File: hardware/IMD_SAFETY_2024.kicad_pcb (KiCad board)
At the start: 4 copper layers, 60 x 40 mm, 4 parts

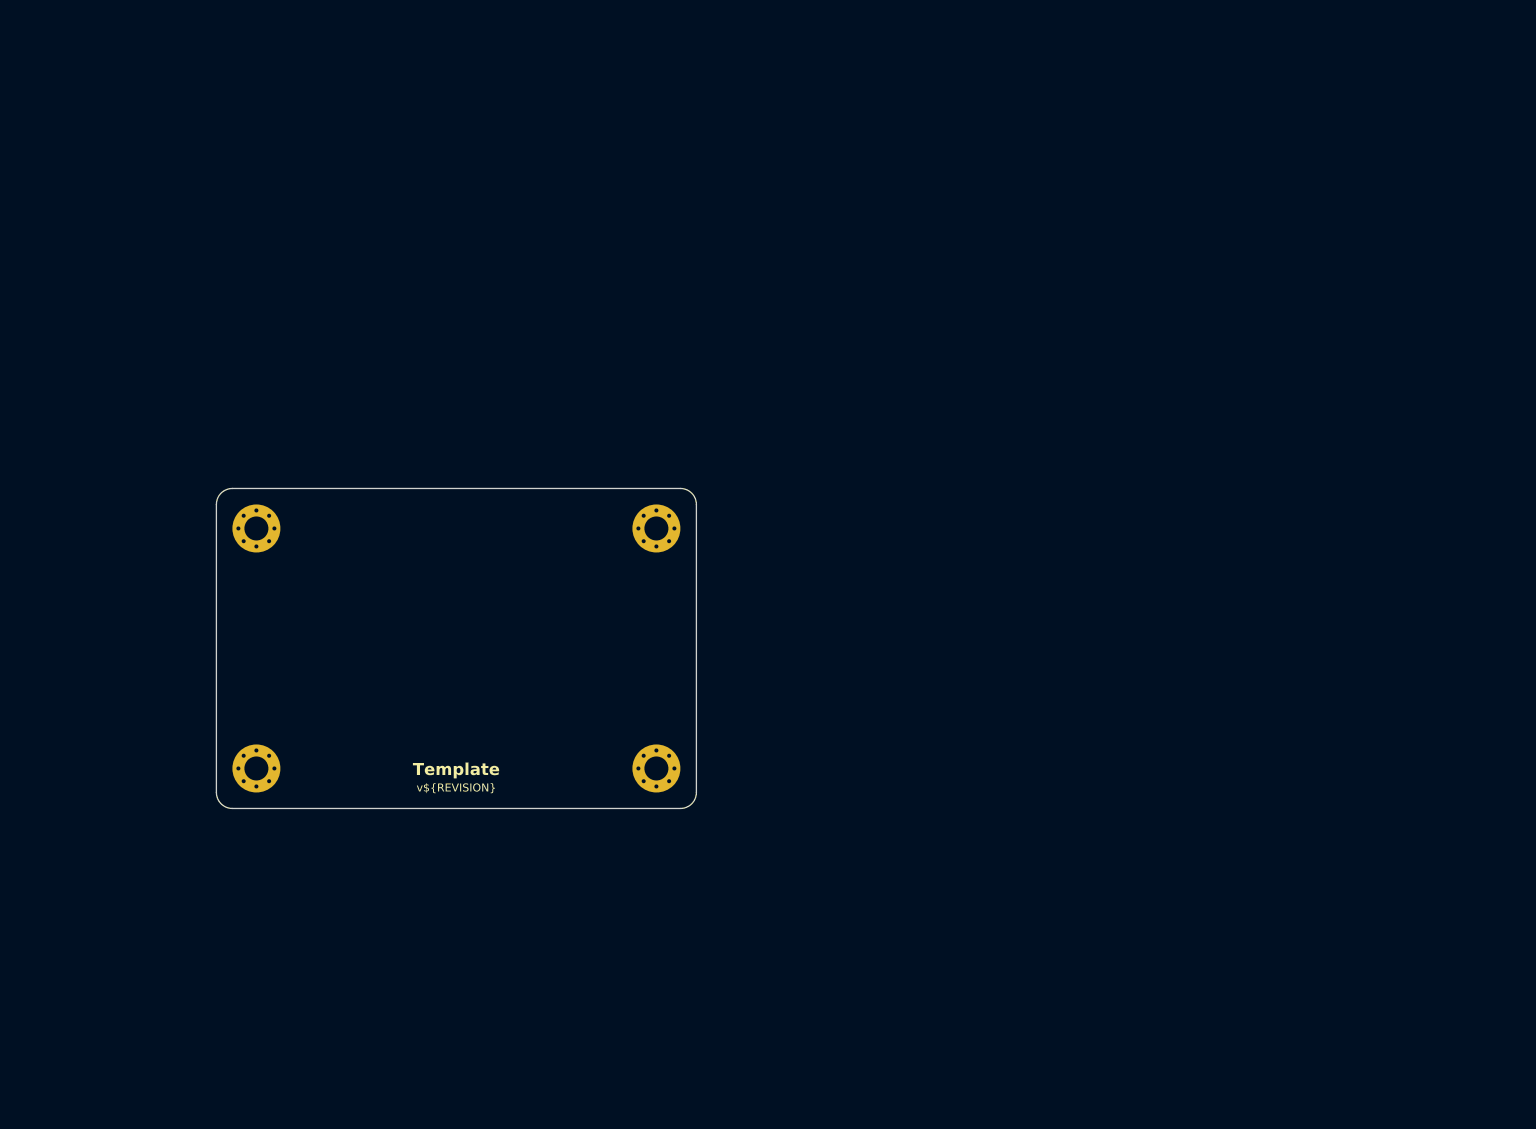
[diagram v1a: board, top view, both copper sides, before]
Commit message: Passives footprint assignment
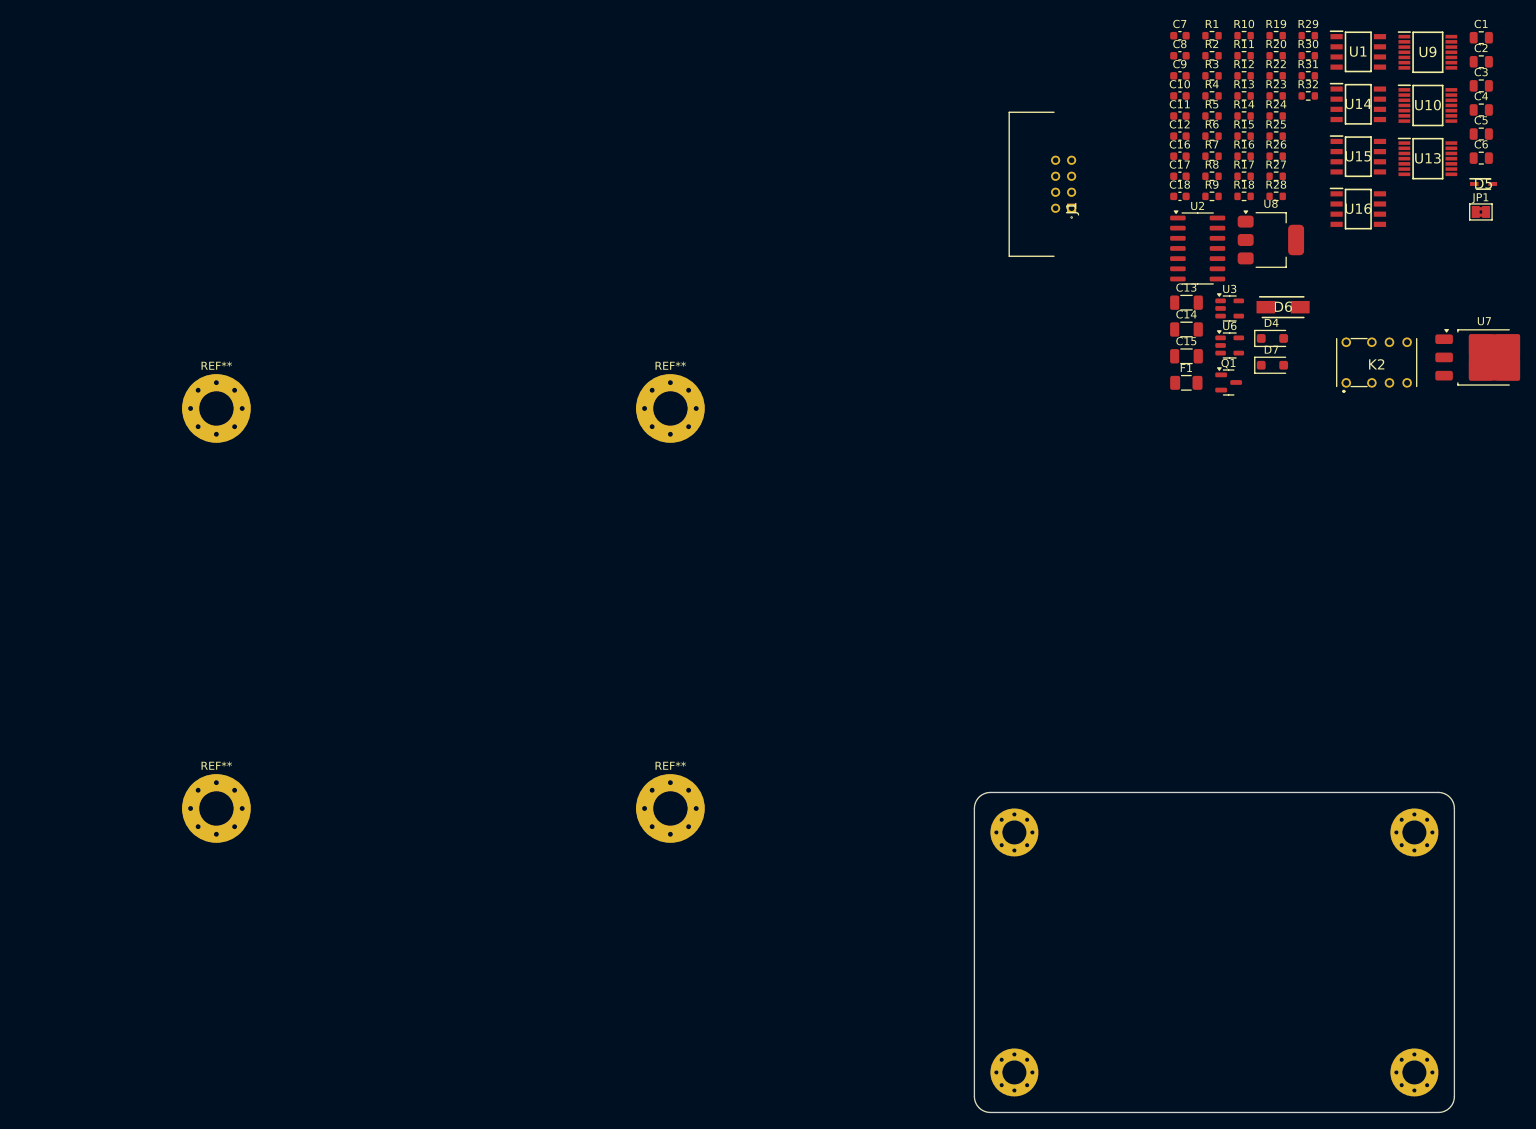
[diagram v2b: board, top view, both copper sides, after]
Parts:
- added C1: 1u/35V, Capacitor_SMD:C_0805_2012Metric, F.Cu at (274.1, 19.7)
- added C10: 100nF/35V, Capacitor_SMD:C_0603_1608Metric, F.Cu at (236.4, 26.9)
- added C11: 100nF/35V, Capacitor_SMD:C_0603_1608Metric, F.Cu at (236.4, 29.4)
- added C12: 100nF/35V, Capacitor_SMD:C_0603_1608Metric, F.Cu at (236.4, 32.0)
- added C13: 47uF, Capacitor_SMD:C_1206_3216Metric, F.Cu at (237.3, 52.8)
- added C14: 22u, Capacitor_SMD:C_1206_3216Metric, F.Cu at (237.3, 56.1)
- added C15: 10u, Capacitor_SMD:C_1206_3216Metric, F.Cu at (237.3, 59.5)
- added C16: 100nF/35V, Capacitor_SMD:C_0603_1608Metric, F.Cu at (236.4, 34.5)
- added C17: 100nF/35V, Capacitor_SMD:C_0603_1608Metric, F.Cu at (236.4, 37.0)
- added C18: 100nF/35V, Capacitor_SMD:C_0603_1608Metric, F.Cu at (236.4, 39.5)
- added C2: 1u/35V, Capacitor_SMD:C_0805_2012Metric, F.Cu at (274.1, 22.7)
- added C3: 1u/35V, Capacitor_SMD:C_0805_2012Metric, F.Cu at (274.1, 25.7)
- added C4: 1u/35V, Capacitor_SMD:C_0805_2012Metric, F.Cu at (274.1, 28.7)
- added C5: 1u/35V, Capacitor_SMD:C_0805_2012Metric, F.Cu at (274.1, 31.7)
- added C6: 1u/35V, Capacitor_SMD:C_0805_2012Metric, F.Cu at (274.1, 34.7)
- added C7: 100nF/35V, Capacitor_SMD:C_0603_1608Metric, F.Cu at (236.4, 19.4)
- added C8: 100nF/35V, Capacitor_SMD:C_0603_1608Metric, F.Cu at (236.4, 21.9)
- added C9: 100nF/35V, Capacitor_SMD:C_0603_1608Metric, F.Cu at (236.4, 24.4)
- added D4: SD103BW, Diode_SMD:D_SOD-123F, F.Cu at (248.0, 57.2)
- added D5: SD24-01FTG, Samacsys:SOD2613X114N, F.Cu at (274.4, 37.9)
- added D6: SK36A-LTP, Samacsys:DIOM5226X244N, F.Cu at (249.3, 53.3)
- added D7: SD103BW, Diode_SMD:D_SOD-123F, F.Cu at (248.0, 60.6)
- added F1: 500mA, Fuse:Fuse_1206_3216Metric, F.Cu at (237.2, 62.8)
- added J1: Main- M80-5300842, Samacsys:M80-53008YY, F.Cu at (222.9, 41.0)
- added JP1: Output_Jumper, Jumper:SolderJumper-2_P1.3mm_Bridged2Bar_Pad1.0x1.5mm, F.Cu at (274.1, 41.4)
- added K2: TE AXICOM IM07DTS, footprints:IM23TS, F.Cu at (261.0, 60.5)
- added Q1: 2N7002, Package_TO_SOT_SMD:SOT-23, F.Cu at (242.5, 62.8)
- added R1: 2.2K, Resistor_SMD:R_0603_1608Metric, F.Cu at (240.5, 19.4)
- added R10: 100k, Resistor_SMD:R_0603_1608Metric, F.Cu at (244.5, 19.4)
- added R11: 14.3k, Resistor_SMD:R_0603_1608Metric, F.Cu at (244.5, 21.9)
- added R12: 150K, Resistor_SMD:R_0603_1608Metric, F.Cu at (244.5, 24.4)
- added R13: 33K, Resistor_SMD:R_0603_1608Metric, F.Cu at (244.5, 26.9)
- added R14: 0k, Resistor_SMD:R_0603_1608Metric, F.Cu at (244.5, 29.4)
- added R15: 400K, Resistor_SMD:R_0603_1608Metric, F.Cu at (244.5, 32.0)
- added R16: 100K, Resistor_SMD:R_0603_1608Metric, F.Cu at (244.5, 34.5)
- added R17: 2.2K, Resistor_SMD:R_0603_1608Metric, F.Cu at (244.5, 37.0)
- added R18: 2.2K, Resistor_SMD:R_0603_1608Metric, F.Cu at (244.5, 39.5)
- added R19: 1K, Resistor_SMD:R_0603_1608Metric, F.Cu at (248.5, 19.4)
- added R2: 2.2K, Resistor_SMD:R_0603_1608Metric, F.Cu at (240.5, 21.9)
- added R20: 10k, Resistor_SMD:R_0603_1608Metric, F.Cu at (248.5, 21.9)
- added R22: 100k, Resistor_SMD:R_0603_1608Metric, F.Cu at (248.5, 24.4)
- added R23: 330R, Resistor_SMD:R_0603_1608Metric, F.Cu at (248.5, 26.9)
- added R24: 20k, Resistor_SMD:R_0603_1608Metric, F.Cu at (248.5, 29.4)
- added R25: 30k, Resistor_SMD:R_0603_1608Metric, F.Cu at (248.5, 32.0)
- added R26: 120k, Resistor_SMD:R_0603_1608Metric, F.Cu at (248.5, 34.5)
- added R27: 20k, Resistor_SMD:R_0603_1608Metric, F.Cu at (248.5, 37.0)
- added R28: 10k, Resistor_SMD:R_0603_1608Metric, F.Cu at (248.5, 39.5)
- added R29: 2.2K, Resistor_SMD:R_0603_1608Metric, F.Cu at (252.5, 19.4)
- added R3: 10K, Resistor_SMD:R_0603_1608Metric, F.Cu at (240.5, 24.4)
- added R30: 100K, Resistor_SMD:R_0603_1608Metric, F.Cu at (252.5, 21.9)
- added R31: 10k, Resistor_SMD:R_0603_1608Metric, F.Cu at (252.5, 24.4)
- added R32: 1M, Resistor_SMD:R_0603_1608Metric, F.Cu at (252.5, 26.9)
- added R4: 10K, Resistor_SMD:R_0603_1608Metric, F.Cu at (240.5, 26.9)
- added R5: 2.2K, Resistor_SMD:R_0603_1608Metric, F.Cu at (240.5, 29.4)
- added R6: 2.2K, Resistor_SMD:R_0603_1608Metric, F.Cu at (240.5, 32.0)
- added R7: 47K, Resistor_SMD:R_0603_1608Metric, F.Cu at (240.5, 34.5)
- added R8: 47K, Resistor_SMD:R_0603_1608Metric, F.Cu at (240.5, 37.0)
- added R9: 300K, Resistor_SMD:R_0603_1608Metric, F.Cu at (240.5, 39.5)
- added REF**: MountingHole_4.3mm_M4_Pad_Via, MountingHole:MountingHole_4.3mm_M4_Pad_Via, F.Cu at (116.0, 66.0)
- added REF**: MountingHole_4.3mm_M4_Pad_Via, MountingHole:MountingHole_4.3mm_M4_Pad_Via, F.Cu at (116.0, 116.0)
- added REF**: MountingHole_4.3mm_M4_Pad_Via, MountingHole:MountingHole_4.3mm_M4_Pad_Via, F.Cu at (172.8, 66.0)
- added REF**: MountingHole_4.3mm_M4_Pad_Via, MountingHole:MountingHole_4.3mm_M4_Pad_Via, F.Cu at (172.8, 116.0)
- added U1: LM393, Samacsys:SOIC127P600X175-8N, F.Cu at (258.7, 21.4)
- added U10: 74HCS08, Samacsys:SOP65P640X120-14N, F.Cu at (267.4, 28.1)
- added U13: 74HC74, Samacsys:SOP65P640X120-14N, F.Cu at (267.4, 34.8)
- added U14: LM393, Samacsys:SOIC127P600X175-8N, F.Cu at (258.7, 28.0)
- added U15: LM393, Samacsys:SOIC127P600X175-8N, F.Cu at (258.7, 34.5)
- added U16: LM393, Samacsys:SOIC127P600X175-8N, F.Cu at (258.7, 41.1)
- added U2: 74AC04SC, Package_SO:SOIC-14_3.9x8.7mm_P1.27mm, F.Cu at (238.7, 46.0)
- added U3: 74LVC1G79, Package_TO_SOT_SMD:SOT-23-5, F.Cu at (242.7, 53.5)
- added U6: 74LVC1G79, Package_TO_SOT_SMD:SOT-23-5, F.Cu at (242.7, 58.1)
- added U7: MC78M12CDTG, Package_TO_SOT_SMD:TO-252-3_TabPin2, F.Cu at (274.5, 59.6)
- added U8: LM1117IMP-5.0, Package_TO_SOT_SMD:SOT-223-3_TabPin2, F.Cu at (247.8, 44.9)
- added U9: 74HCS32, Samacsys:SOP65P640X120-14N, F.Cu at (267.4, 21.5)
- moved REF** 102.1 mm to (265.8, 119.0)
- moved REF** 102.1 mm to (215.8, 149.0)
- moved REF** 102.1 mm to (215.8, 119.0)
- moved REF** 102.1 mm to (265.8, 149.0)
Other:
- board text added: "BETWEEN HORIZONTAL HOLES: 56,75mm"
- board text added: "BETWEEN VERTICAL HOLES: 50mm"
- board text removed: "Template"
- board text removed: "v${REVISION}"

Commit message: WIP Layout
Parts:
- removed the REF** at (265.8, 119.0)
- removed the REF** at (215.8, 149.0)
- removed the REF** at (215.8, 119.0)
- removed the REF** at (265.8, 149.0)
- added C19: 100nF/35V, Capacitor_SMD:C_0603_1608Metric, F.Cu at (136.7, 93.1)
- added C20: 100nF/35V, Capacitor_SMD:C_0603_1608Metric, F.Cu at (130.2, 92.9)
- added C21: TBD, Capacitor_SMD:C_1206_3216Metric, F.Cu at (146.4, 81.2)
- added R33: 10k, Resistor_SMD:R_0603_1608Metric, F.Cu at (115.6, 85.0)
- added R34: 10k, Resistor_SMD:R_0603_1608Metric, F.Cu at (115.6, 83.0)
- added REF**: PinHeader_1x10_P2.54mm_Vertical, Connector_PinHeader_2.54mm:PinHeader_1x10_P2.54mm_Vertical, F.Cu at (133.4, 117.4)
- added TP1: TestPoint_Small, TestPoint:TestPoint_Pad_D1.0mm, F.Cu at (92.6, 76.2)
- added TP10: TestPoint_Small, TestPoint:TestPoint_Pad_D1.0mm, F.Cu at (101.8, 76.2)
- added TP11: TestPoint_Small, TestPoint:TestPoint_Pad_D1.0mm, F.Cu at (101.8, 79.2)
- added TP12: TestPoint_Small, TestPoint:TestPoint_Pad_D1.0mm, F.Cu at (101.8, 82.3)
- added TP13: TestPoint_Small, TestPoint:TestPoint_Pad_D1.0mm, F.Cu at (104.8, 76.2)
- added TP14: TestPoint_Small, TestPoint:TestPoint_Pad_D1.0mm, F.Cu at (104.8, 79.2)
- added TP15: TestPoint_Small, TestPoint:TestPoint_Pad_D1.0mm, F.Cu at (104.8, 82.3)
- added TP2: TestPoint_Small, TestPoint:TestPoint_Pad_D1.0mm, F.Cu at (92.6, 79.2)
- added TP3: TestPoint_Small, TestPoint:TestPoint_Pad_D1.0mm, F.Cu at (92.6, 82.3)
- added TP4: TestPoint_Small, TestPoint:TestPoint_Pad_D1.0mm, F.Cu at (95.7, 76.2)
- added TP5: TestPoint_Small, TestPoint:TestPoint_Pad_D1.0mm, F.Cu at (95.7, 79.2)
- added TP6: TestPoint_Small, TestPoint:TestPoint_Pad_D1.0mm, F.Cu at (95.7, 82.3)
- added TP7: TestPoint_Small, TestPoint:TestPoint_Pad_D1.0mm, F.Cu at (98.7, 76.2)
- added TP8: TestPoint_Small, TestPoint:TestPoint_Pad_D1.0mm, F.Cu at (98.7, 79.2)
- added TP9: TestPoint_Small, TestPoint:TestPoint_Pad_D1.0mm, F.Cu at (98.7, 82.3)
- JP1: footprint Jumper:SolderJumper-2_P1.3mm_Bridged2Bar_Pad1.0x1.5mm -> Jumper:SolderJumper-2_P1.3mm_Open_Pad1.0x1.5mm
- moved U9 165.4 mm to (121.2, 98.8), turned to 180 degrees
- moved U10 159.3 mm to (121.2, 91.2), turned to 180 degrees
- moved U13 154.2 mm to (121.2, 83.7), turned to 180 degrees
- moved C1 149.2 mm to (149.6, 101.8)
- moved JP1 147.3 mm to (134.2, 87.6), turned to 180 degrees
- moved C2 142.4 mm to (150.4, 93.2), turned to 90 degrees
- moved C9 140.8 mm to (119.2, 102.4)
- moved R32 136.4 mm to (128.8, 84.6), turned to -90 degrees
- moved C8 133.5 mm to (135.0, 108.7), turned to 180 degrees
- moved R28 130.9 mm to (127.3, 89.0)
- moved R30 130.9 mm to (132.5, 74.2), turned to 180 degrees
- moved C18 129.6 mm to (119.2, 94.8)
- moved R22 129.5 mm to (134.2, 85.4)
- moved R29 129.2 mm to (135.5, 74.2), turned to 180 degrees
- moved R19 128.9 mm to (156.0, 109.2)
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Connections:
- net Net-(D4-K) renamed /~{CLR}
- net Net-(U10-Pad3) renamed /DUTY&FREQ_OK
- C12 pad 1: +24V -> +5V
- C16 pad 1: +24V -> +5V
- J1 pad 5: COCKPIT_LED -> GND
- J1 pad 6: GND -> COCKPIT_LED
- U1 pad 8: +24V -> +5V
- U10 pad 10: (no net) -> GND
- U10 pad 11: (no net) -> unconnected-(U10-Pad11)
- U10 pad 12: (no net) -> GND
- U10 pad 13: (no net) -> GND
- U10 pad 4: (no net) -> GND
- U10 pad 5: (no net) -> GND
- U10 pad 6: (no net) -> unconnected-(U10-Pad6)
- U10 pad 8: (no net) -> unconnected-(U10-Pad8)
- U10 pad 9: (no net) -> GND
- U13 pad 10: (no net) -> Net-(U13B-~{S})
- U13 pad 11: (no net) -> GND
- U13 pad 12: (no net) -> GND
- U13 pad 13: (no net) -> Net-(U13B-~{R})
- U13 pad 8: (no net) -> unconnected-(U13B-~{Q}-Pad8)
- U13 pad 9: (no net) -> unconnected-(U13B-Q-Pad9)
- U16 pad 8: +24V -> +5V
- U2 pad 10: (no net) -> unconnected-(U2-Pad10)
- U2 pad 11: (no net) -> GND
- U2 pad 12: (no net) -> unconnected-(U2-Pad12)
- U2 pad 13: (no net) -> GND
- U2 pad 8: (no net) -> unconnected-(U2-Pad8)
- U2 pad 9: (no net) -> GND
- U9 pad 10: (no net) -> GND
- U9 pad 11: (no net) -> unconnected-(U9-Pad11)
- U9 pad 12: (no net) -> GND
- U9 pad 13: (no net) -> GND
- U9 pad 4: (no net) -> GND
- U9 pad 5: (no net) -> GND
- U9 pad 6: (no net) -> unconnected-(U9-Pad6)
- U9 pad 8: (no net) -> unconnected-(U9-Pad8)
- U9 pad 9: (no net) -> GND
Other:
- board size 60 x 40 mm -> 66.8 x 60 mm
- board text added: "Logic analyzer test points"
- board text added: "Right side of the ISOMETER compatibility"

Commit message: WIP Routing
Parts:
- moved TP1 74.6 mm to (165.8, 90.4)
- moved TP2 74.4 mm to (165.8, 92.6)
- moved TP6 71.6 mm to (161.6, 110.2)
- moved TP8 67.4 mm to (161.6, 103.6)
- moved TP7 67.1 mm to (158.8, 106.0)
- moved TP12 61.3 mm to (161.2, 97.2)
- moved TP5 54.9 mm to (146.6, 99.6)
- moved TP3 52.6 mm to (145.2, 82.2)
- moved TP11 52.1 mm to (146.6, 105.8)
- moved TP4 52.1 mm to (147.4, 82.2)
- moved TP9 46.6 mm to (143.4, 95.4)
- moved TP10 44.1 mm to (144.4, 87.7)
- moved TP14 36.8 mm to (132.2, 103.8)
- moved TP15 35.2 mm to (139.6, 87.8)
- moved TP13 33.3 mm to (132.0, 95.4)
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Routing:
- net DUTY_OK: track 0.00 -> 64.2 mm
- net Net-(U16B--): track 0.00 -> 37.3 mm, vias 0 -> 3
- net /NMOS_IN: track 0.00 -> 25.8 mm
- net Net-(U16A-+): track 0.00 -> 24.4 mm
- net /~{CLR}: track 0.00 -> 22.3 mm
- net IMD_OK_HS: track 0.00 -> 22.3 mm
- net PWM_FREQ_OK: track 0.00 -> 19.5 mm
- net Net-(U15A-+): track 0.00 -> 18.8 mm
- net /Q_DFF: track 0.00 -> 16.3 mm
- net IMD_PWM_LS: track 0.00 -> 15.3 mm
- net Net-(U3-Q): track 0.00 -> 14.1 mm
- net Net-(U16A--): track 0.00 -> 13.8 mm
- net Net-(D6-A): track 0.00 -> 13.7 mm
- net Net-(U15A--): track 0.00 -> 12.7 mm
- net Net-(U15B--): track 0.00 -> 12.4 mm
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
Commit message: 0xDRC, ready for review
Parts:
- moved TP9 19.0 mm to (161.2, 88.8)
- moved TP10 7.96 mm to (143.6, 95.6)
- moved TP15 7.92 mm to (138.2, 95.6)
- moved C15 3.53 mm to (137.8, 80.4), turned to 90 degrees
- moved R29 3.46 mm to (133.4, 78.8), turned to -90 degrees
- moved R30 3.39 mm to (133.4, 81.8), turned to -90 degrees
- moved C6 1.85 mm to (156.2, 71.4), turned to -90 degrees
- moved C3 1.00 mm to (166.4, 71.8), turned to 180 degrees
- moved R31 1.00 mm to (128.0, 82.6), turned to -90 degrees
- moved C20 0.82 mm to (137.4, 91.4)
- moved C7 0.22 mm to (158.8, 72.3)
- moved D4 0.22 mm to (135.5, 80.4), turned to 90 degrees
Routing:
- net GND: track 3.22 -> 110.0 mm, vias 2 -> 60
- net RESET: track 5.31 -> 105.9 mm, vias 0 -> 2
- net COCKPIT_LED: track 0.00 -> 87.8 mm, vias 0 -> 1
- net OK_HS_TTL: track 4.16 -> 65.7 mm, vias 0 -> 2
- net +24V: track 9.16 -> 67.6 mm
- net /Q_DFF: track 16.3 -> 73.2 mm, vias 0 -> 1
- net SDC_OUT: track 0.00 -> 52.7 mm
- net SDC_IN: track 0.00 -> 49.2 mm
- net /DUTY&FREQ_OK: track 10.7 -> 51.9 mm
- net /~{CLR}: track 22.3 -> 60.0 mm, vias 0 -> 1
- net PWM_TTL: track 1.94 -> 38.1 mm, vias 0 -> 3
- net PWM_FREQ_OK: track 19.5 -> 53.3 mm, vias 0 -> 1
- net +12V: track 2.83 -> 27.9 mm
- net Net-(D4-A): track 3.61 -> 26.8 mm, vias 0 -> 2
- net Net-(U6-D): track 7.91 -> 28.3 mm, vias 0 -> 2
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- added copper zone on F.Cu, net +5V
- added copper zone on In2.Cu, net +5V
- added copper zone on B.Cu, net GND
- added copper zone on In1.Cu, net GND
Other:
- board text added: "Stackup: F.Cu - SIG/PWR In1.Cu - GND In2.Cu -PWR B.Cu SIG/GND"

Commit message: Production Files
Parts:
- added G***: LOGO, Logos:PUTM_LOGO_15mm, F.Cu at (128.0, 112.3)
- added G***: LOGO, Logos:SignatureBox25mm, B.Cu at (155.4, 80.6)
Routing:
- net Net-(U3-Q): track 27.3 -> 28.6 mm
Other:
- board text added: "HARDWARE REVISION 2.0.0"
- board text added: "Przemysław Zioła Szymon Sambor"
